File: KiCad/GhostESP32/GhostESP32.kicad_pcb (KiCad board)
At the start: 2 copper layers, 50 x 50 mm, 40 parts, among them P1 USB_OTG, P2 CONN_02X30, Q1 Q_NPN_BCE, Q2 Q_NPN_BCE, SW1 SW_Push, SW2 SW_Push, U1 MC33269, U2 LM358, U3 CP2102, U4 ESP-WROOM-32

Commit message: Spent hours doing routing...
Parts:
- moved R10 38.7 mm to (132.0, 116.0)
- moved U2 36.0 mm to (141.6, 114.1)
- moved D1 34.2 mm to (127.9, 81.5), turned to 0 degrees
- moved D4 32.5 mm to (131.9, 112.3)
- moved Q1 31.5 mm to (134.2, 85.4)
- moved R4 31.4 mm to (154.8, 113.3), turned to 0 degrees
- moved R1 29.4 mm to (128.0, 78.9), turned to 180 degrees
- moved R8 25.1 mm to (135.2, 110.1)
- moved R2 22.3 mm to (134.3, 90.1), turned to 180 degrees
- moved C6 19.8 mm to (170.1, 77.0), turned to 0 degrees
- moved C8 19.6 mm to (126.7, 101.8)
- moved R5 18.5 mm to (154.8, 110.8), turned to 0 degrees
- moved R7 18.2 mm to (150.2, 113.7), turned to 90 degrees
- moved C9 13.4 mm to (126.8, 104.2)
- moved D3 11.0 mm to (131.9, 110.1)
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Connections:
- P2 pad 1: +3V3 -> SENSOR_VP
- P2 pad 10: +5V -> Net-(P2-Pad10)
- P2 pad 11: IO23 -> GND
- P2 pad 13: IO22 -> GND
- P2 pad 15: IO17 -> GND
- P2 pad 17: IO16 -> Net-(P2-Pad17)
- P2 pad 18: IO12 -> USB_SUSPEND
- P2 pad 19: IO5 -> Net-(P2-Pad19)
- P2 pad 2: +5V -> +3V3
- P2 pad 20: IO14 -> +5V
- P2 pad 21: IO4 -> +5V
- P2 pad 22: IO27 -> +5V
- P2 pad 23: IO0 -> +5V
- P2 pad 24: IO26 -> +5V
- P2 pad 25: IO18 -> Net-(P2-Pad25)
- P2 pad 26: IO25 -> GND
- P2 pad 27: IO19 -> GND
- P2 pad 28: IO33 -> GND
- P2 pad 29: IO21 -> GND
- P2 pad 30: IO32 -> GND
- P2 pad 31: SENSOR_VN -> IO23
- P2 pad 32: IO35 -> IO22
- P2 pad 33: SENSOR_VP -> IO21
- P2 pad 34: IO34 -> IO19
- P2 pad 35: GND -> IO18
- P2 pad 36: GND -> IO5
- P2 pad 37: GND -> IO17
- P2 pad 38: GND -> IO16
- P2 pad 39: GND -> IO4
- P2 pad 4: +5V -> +3V3
- P2 pad 40: GND -> IO0
- P2 pad 41: SD1 -> GND
- P2 pad 42: USB_SUSPEND -> IO2
- P2 pad 43: SD0 -> IO15
- P2 pad 44: Net-(P2-Pad44) -> SD1
- P2 pad 45: SD2 -> SD0
- P2 pad 46: Net-(P2-Pad46) -> CLK
- P2 pad 47: SD3 -> CMD
- P2 pad 48: Net-(P2-Pad48) -> SD3
- P2 pad 49: CMD -> SD2
- P2 pad 51: CLK -> IO12
- P2 pad 52: Net-(P2-Pad52) -> IO14
- P2 pad 53: IO15 -> IO27
- P2 pad 54: Net-(P2-Pad54) -> IO26
- P2 pad 55: IO2 -> IO25
- P2 pad 56: Net-(P2-Pad56) -> IO33
- P2 pad 57: Net-(P2-Pad57) -> IO32
- P2 pad 58: Net-(P2-Pad58) -> IO35
- P2 pad 59: Net-(P2-Pad59) -> IO34
- P2 pad 6: +5V -> Net-(P2-Pad6)
- P2 pad 60: Net-(P2-Pad60) -> SENSOR_VN
- P2 pad 7: GND -> +5V
- P2 pad 9: GND -> +5V
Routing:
- net EN: track 13.9 -> 60.8 mm, vias 0 -> 4
- net IO34: track 0.00 -> 32.0 mm
- net IO23: track 0.00 -> 31.1 mm
- net IO22: track 0.00 -> 29.5 mm
- net +3V3: track 72.5 -> 43.9 mm
- net GND: track 0.00 -> 28.0 mm
- net IO35: track 0.00 -> 24.0 mm
- net IO19: track 0.00 -> 22.9 mm
- net RTS: track 0.00 -> 22.8 mm
- net IO18: track 0.00 -> 21.5 mm
- net IO33: track 0.00 -> 21.1 mm
- net IO5: track 0.00 -> 20.1 mm
- net IO25: track 0.00 -> 19.8 mm
- net IO17: track 0.00 -> 19.5 mm
- net IO26: track 0.00 -> 18.4 mm
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
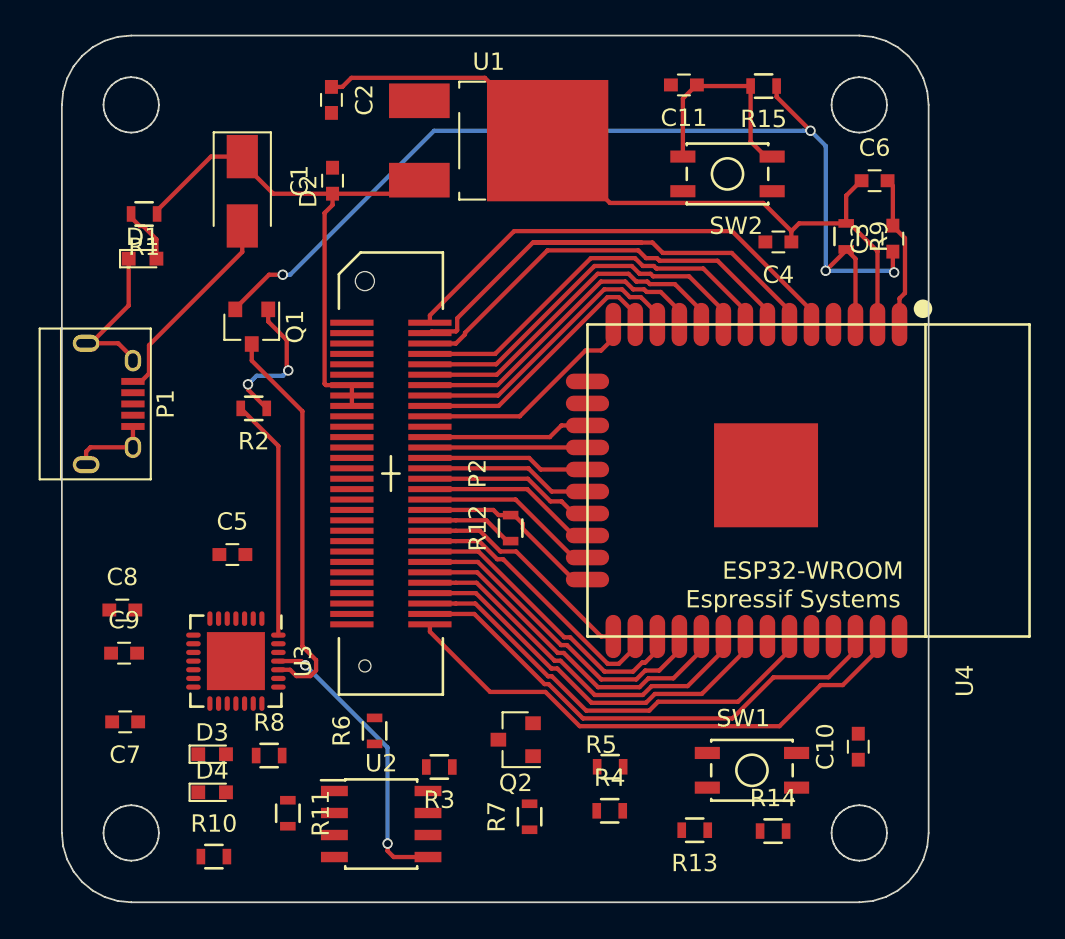
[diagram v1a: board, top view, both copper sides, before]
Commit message: GhostESP32 and GhostSensorboard mostly done - but with wrong 60 pin connector
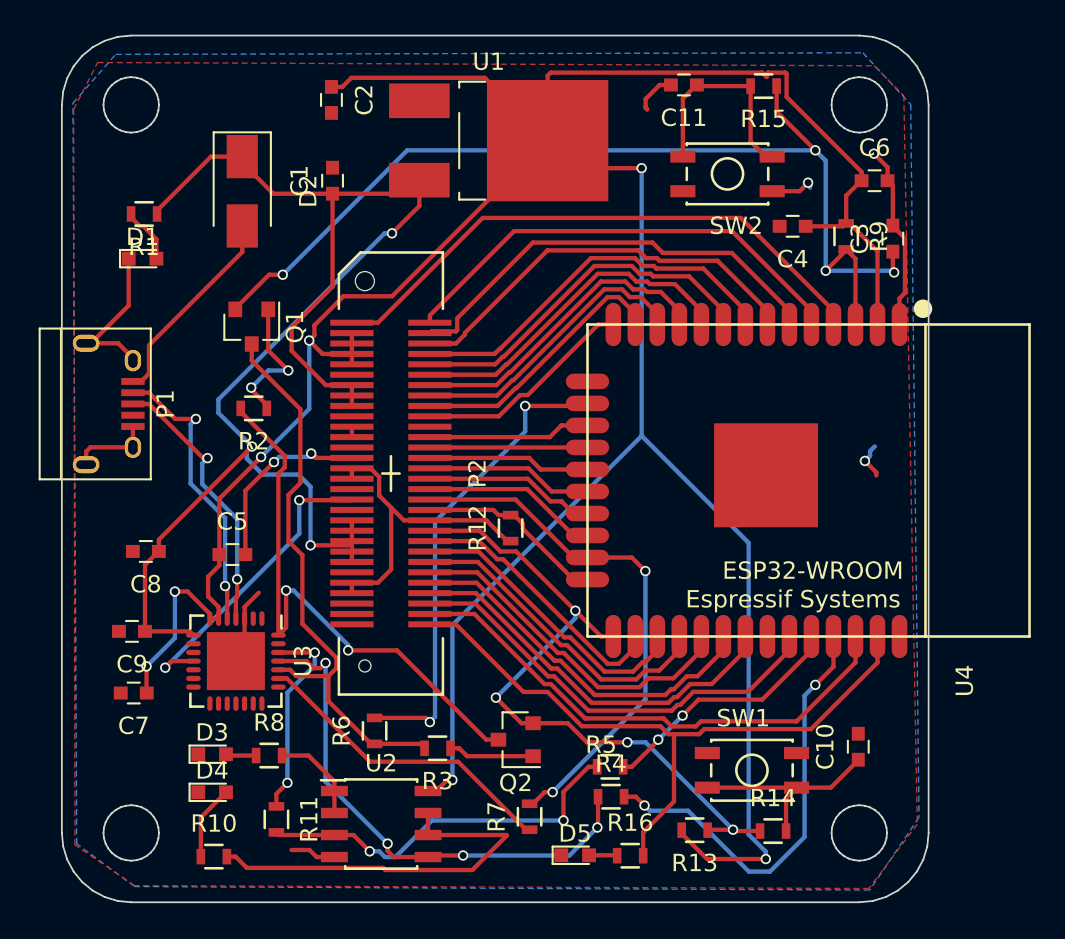
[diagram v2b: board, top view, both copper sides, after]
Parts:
- added D5: LED, LEDs:LED_0603, F.Cu at (152.8, 115.9)
- added R16: 330, Resistors_SMD:R_0603, F.Cu at (156.0, 115.9)
- moved C8 3.64 mm to (128.1, 98.4), turned to 180 degrees
- moved C7 1.74 mm to (127.4, 106.5)
- moved C9 1.34 mm to (127.3, 103.0), turned to 180 degrees
- moved C4 1.22 mm to (165.4, 79.6)
- moved R3 1.08 mm to (144.9, 109.7)
- moved R4 0.82 mm to (154.9, 112.5)
- moved R11 0.75 mm to (135.6, 113.8)
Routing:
- net +3V3: track 43.9 -> 184.7 mm, vias 0 -> 7
- net +5V: track 32.0 -> 84.3 mm, vias 0 -> 3
- net GND: track 28.0 -> 66.6 mm, vias 0 -> 4
- net SENSOR_VP: track 0.00 -> 33.3 mm
- net IO13: track 0.00 -> 27.5 mm, vias 0 -> 2
- net IO0: track 13.1 -> 39.9 mm, vias 0 -> 4
- net TXD0: track 0.00 -> 26.1 mm, vias 0 -> 2
- net Net-(R10-Pad2): track 0.00 -> 23.1 mm
- net TXD: track 0.00 -> 22.2 mm, vias 0 -> 2
- net IO15: track 10.5 -> 30.7 mm, vias 0 -> 2
- net DTR: track 14.0 -> 33.0 mm, vias 0 -> 2
- net CTS: track 0.00 -> 18.1 mm
- net USB_SUSPEND: track 0.00 -> 17.7 mm, vias 0 -> 2
- net USB_DN: track 0.00 -> 16.8 mm, vias 0 -> 2
- net USB_DP: track 0.00 -> 15.8 mm, vias 0 -> 2
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- added copper zone on B.Cu, net GND
- added copper zone on F.Cu, net GND
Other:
- board text added: "GhostESP32 ESP-WROOM-32 Frode Lillerud, 11.feb 2017"

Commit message: Both boards done, and sent to Elecrow.
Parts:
- Q1, Q2: value Q_NPN_BCE -> Q_NPN_BEC
- R16: value 330 -> 390
- renumbered D1 to POWER, D4 to RX, D3 to TX
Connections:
- Q1 pad 2: EN -> RTS
- Q1 pad 3: RTS -> EN
- Q2 pad 2: IO0 -> DTR
- Q2 pad 3: DTR -> IO0
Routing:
- net IO0: track 39.9 -> 48.1 mm, vias 4 -> 3
- net EN: track 60.6 -> 64.5 mm
- net RTS: track 33.1 -> 36.1 mm, vias 0 -> 4
- net (no net): track 2.19 -> 0.00 mm, vias 1 -> 0
- net DTR: track 33.0 -> 31.4 mm, vias 2 -> 0
- net Net-(R11-Pad1): track 11.9 -> 12.8 mm
- net USB_DN: track 16.8 -> 16.2 mm
